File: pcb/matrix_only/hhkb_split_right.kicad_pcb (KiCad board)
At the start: 2 copper layers, 171.7 x 97.4 mm, 83 parts, among them SW1 CPG151101S11-2, SW10 CPG151101S11-2, SW11 CPG151101S11-2, SW12 CPG151101S11-2, SW13 CPG151101S11-2, SW14 CPG151101S11-2, SW15 CPG151101S11-2, SW16 CPG151101S11-2, SW17 CPG151101S11-2, SW18 CPG151101S11-2, SW19 CPG151101S11-2, SW2 CPG151101S11-2, SW20 CPG151101S11-2, SW21 CPG151101S11-2, SW22 CPG151101S11-2, SW23 CPG151101S11-2, SW24 CPG151101S11-2, SW25 CPG151101S11-2, SW26 CPG151101S11-2, SW27 CPG151101S11-2, SW28 CPG151101S11-2, SW29 CPG151101S11-2, SW3 CPG151101S11-2, SW30 CPG151101S11-2, SW31 CPG151101S11-2, SW32 CPG151101S11-2, SW33 CPG151101S11-2, SW34 CPG151101S11-2, SW4 CPG151101S11-2, SW5 CPG151101S11-2, SW6 CPG151101S11-2, SW7 CPG151101S11-2, SW8 CPG151101S11-2, SW9 CPG151101S11-2, U1 74LVC595, U2 74LVC595

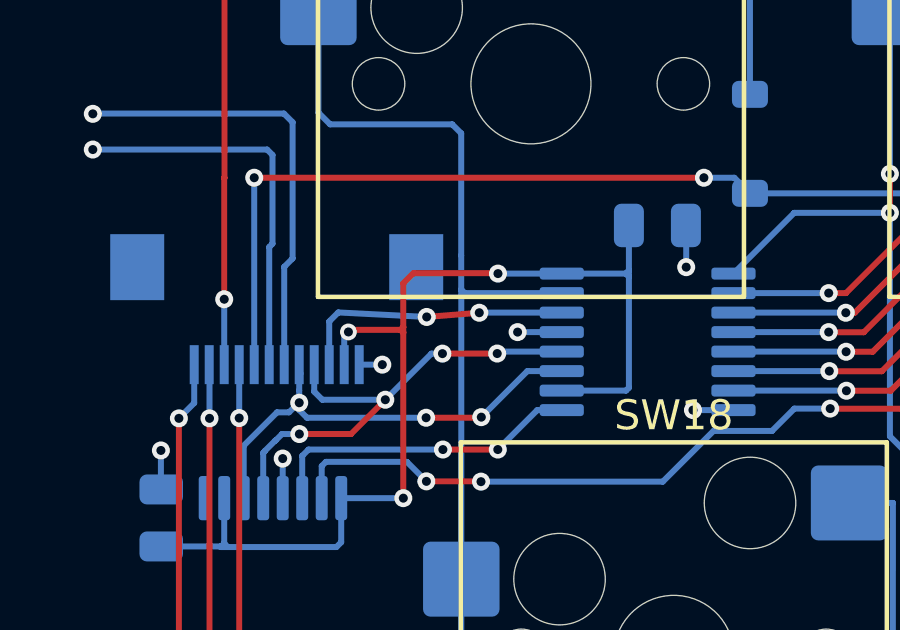
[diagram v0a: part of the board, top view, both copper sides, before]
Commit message: #49 左の SCK・CS・V3V3 にも露出ビア（利用者）。露出は左右の全ネットがビアに。3 基板 DRC 0・検査 460 緑
Co-Authored-By: Claude Fable 5 <noreply@anthropic.com>
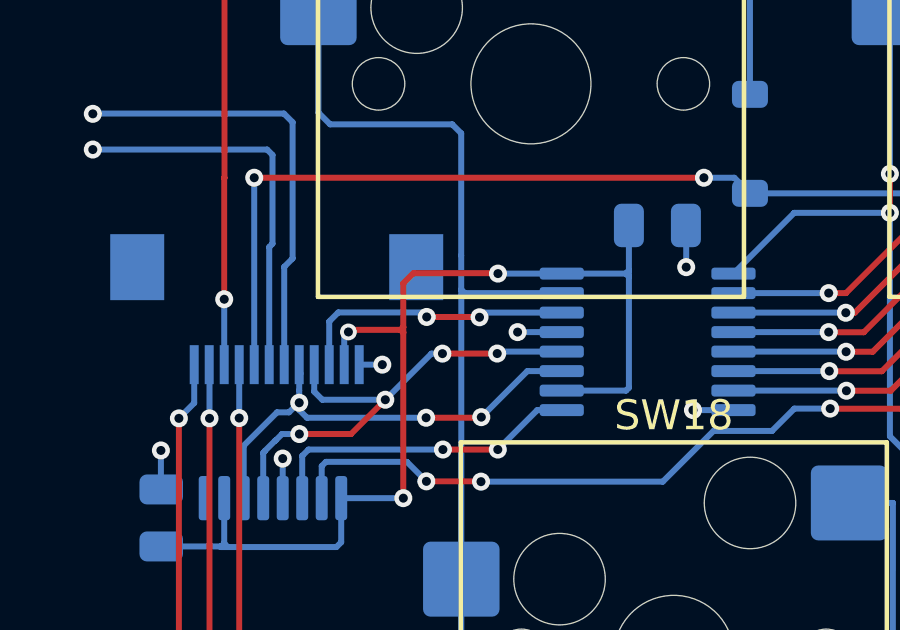
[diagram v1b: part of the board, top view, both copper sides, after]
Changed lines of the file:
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@@
 	(segment
 		(start 79.85 88.72)
-		(end 79.85 88.72)
+		(end 81.6 88.72)
+		(width 0.2)
+		(layer "F.Cu")
+		(net "SPI_MOSI")
+	)
+	(segment
+		(start 81.6 88.72)
+		(end 81.61 88.73)
 		(width 0.2)
 		(layer "F.Cu")
@@
 	(segment
 		(start 79.85 88.72)
-		(end 81.6025 88.58)
+		(end 79.85 88.72)
 		(width 0.2)
 		(layer "F.Cu")
@@
 	)
 	(via
-		(at 81.6025 88.58)
+		(at 81.61 88.73)
 		(size 0.6)
 		(drill 0.3)
@@
 	)
 	(segment
-		(start 76.6 90.309999)
-		(end 76.599999 90.31)
+		(start 79.7 88.57)
+		(end 79.85 88.72)
 		(width 0.2)
 		(layer "B.Cu")
@@
 	)
 	(segment
-		(start 81.815 88.575)
-		(end 84.3505 88.575)
-		(width 0.2)
-		(layer "B.Cu")
-		(net "SPI_MOSI")
-	)
-	(segment
-		(start 81.81 88.58)
-		(end 81.815 88.575)
+		(start 76.6 90.309999)
+		(end 76.599999 90.31)
 		(width 0.2)
 		(layer "B.Cu")
@@
 	)
 	(segment
-		(start 79.85 88.72)
-		(end 76.902182 88.57)
+		(start 81.765 88.575)
+		(end 84.3505 88.575)
 		(width 0.2)
 		(layer "B.Cu")
@@
 	)
 	(segment
-		(start 81.6025 88.58)
-		(end 81.81 88.58)
+		(start 81.61 88.73)
+		(end 81.765 88.575)
 		(width 0.2)
 		(layer "B.Cu")
+		(net "SPI_MOSI")
+	)
+	(segment
+		(start 76.902182 88.57)
+		(end 79.7 88.57)
+		(width 0.2)
+		(layer "B.Cu")

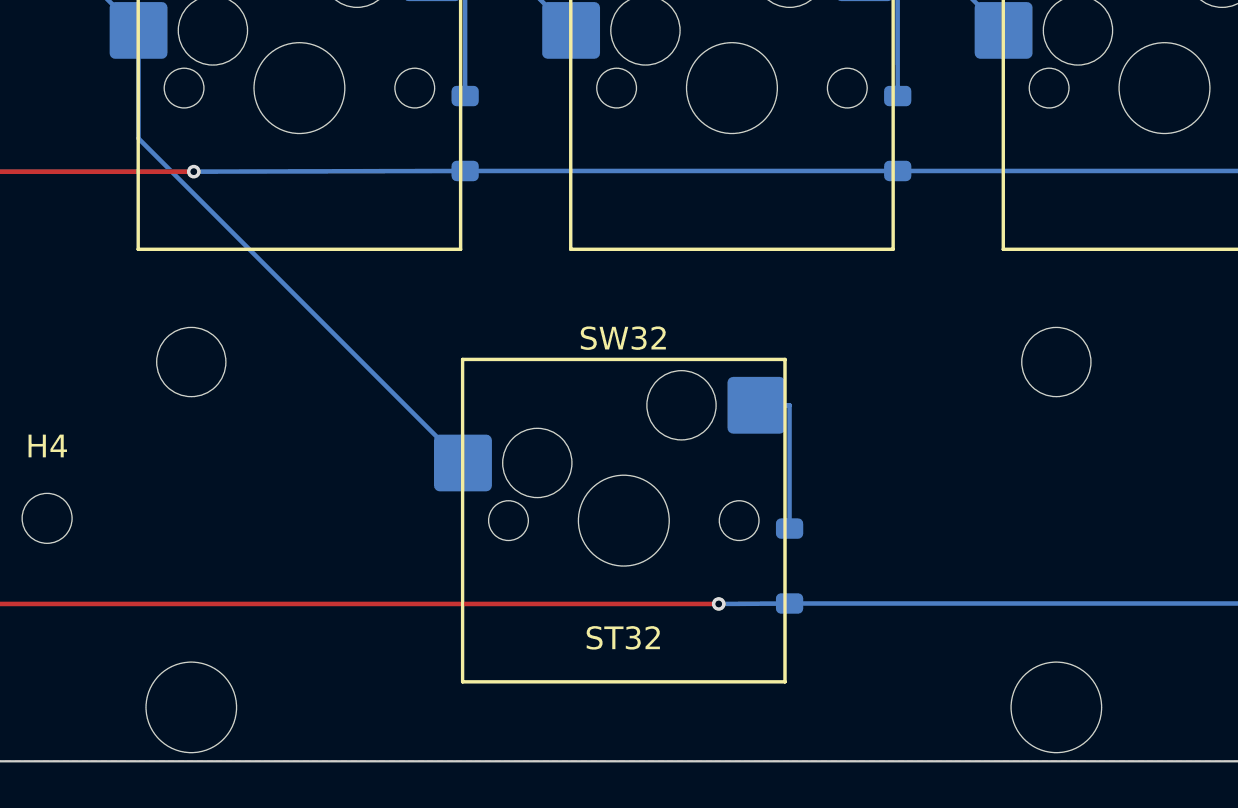
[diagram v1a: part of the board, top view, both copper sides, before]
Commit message: スペースキー 2.75u 化を基板まで反映（3 基板とも DRC 0 / 未配線 0）
設計側（29f4471）に続き、基板を作り直した。

**matrix_only のスペースキーを 2.75u へ**（KiCad の API で差し替え）:
- SW27/SW32 → SW_Hotswap_Kailh_MX_2.75u
- ST27/ST32 → Stabilizer_Cherry_MX_2.00u（穴が ±19.05 → ±11.938）
- SW/ST/D を x 左 −2.38125 / 右 +2.38125 だけ移動

**配線**: ダイオード側 2 本ずつは平行移動で端点がパッドに 0.0001mm 一致。
COL は経路の形が変わるので引き直した（左 COL3・右 COL0）。
⚠️ **利用者の指摘「col0 の配線が規則的じゃない」「col3 も」で 1 度やり直した。**
最初はクリアランスだけ見て 71.9°/2.6°/28.1°/82.9° の半端な角度で引いており、
**この板の他の配線は全部 0°/45°/90°/135°** だった。
縦→45°→水平の 3 区間に作り直し、角度を 45° の倍数に固定したまま
総当たりで障害物との距離が最大の経路を選んだ（左 +0.656mm / 右 +1.650mm）。

**シルクが 0.12mm のまま残っていたのも直した**（gen_pcb の仕上げを
通らないため。→ pcb-routing-handover.md に落とし穴として記録）。

検証: 3 基板とも 違反 0 / 未配線 0。スタビ 4 個すべて ±11.938。
STL のハウジング間隔を実測して 23.880mm（=2u）を確認。
fab_check（595 48 パッド / XIAO 14 パッド / 61 キー経路）全 OK。
基板の外形は不変（左 138.363×97.4 / 右 171.70×97.4 / 子 21.0×32.0）。
検査 464 緑。

記録: スタビの節を 2.75u 前提に書き直し、国内入手性の調査結果
（2u は潤沢・3u は買えない）と、FFC コネクタ C88360 の在庫が
40 日で 0 になるペースであることを追記。#46 の古い「次の一手」も直した。

Co-Authored-By: Claude Opus 5 (1M context) <noreply@anthropic.com>
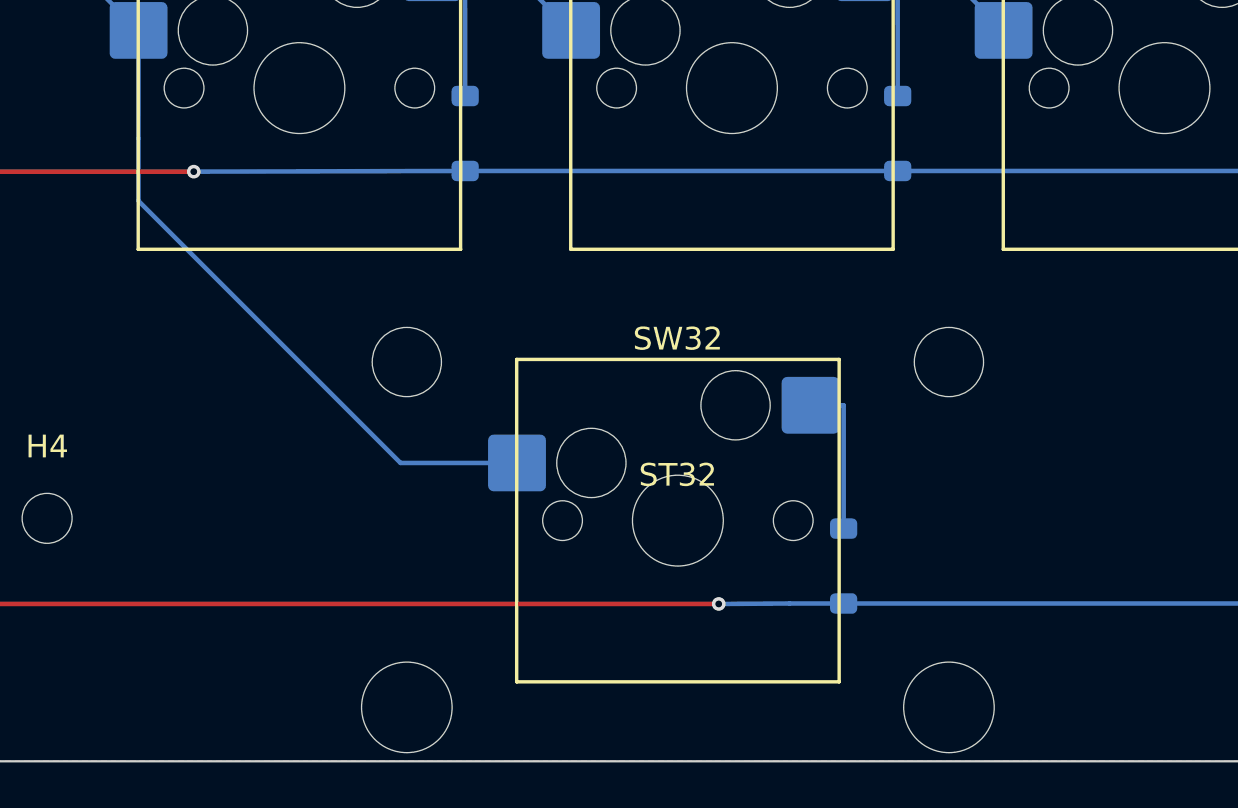
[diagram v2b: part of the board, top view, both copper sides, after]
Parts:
- ST32: value Stabilizer_Cherry_MX_3.00u -> Stabilizer_Cherry_MX_2.00u; footprint Stabilizer_Cherry_MX_3.00u -> Stabilizer_Cherry_MX_2.00u
- SW32: footprint SW_Hotswap_Kailh_MX_3.00u -> SW_Hotswap_Kailh_MX_2.75u
- moved D32 2.38 mm to (121.6, 140.1)
- moved ST32 2.38 mm to (114.3, 138.1)
- moved SW32 2.38 mm to (114.3, 138.1)
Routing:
- net COL0: track 97.9 -> 101.9 mm

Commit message: #53 決着: スペースのスタビ 2 個を 180°（ワイヤ奥）に回す。大穴が板前縁まで 0.381mm だったのが小穴 2.14mm に。interface.stab_flipped を gen_pcb・gen_plate・find_mounts が見る。matrix_only の ST27/ST32 を回して手順どおり再生成、3 基板 DRC 0・警告数不変。NPTH の縁 ≥1.0mm の検査を足し、回す前の板で 0.381 を検出することを確認。実形状のスタビ開口検査・test_assembly 69 件・高速 387 件緑
Co-Authored-By: Claude Fable 5 <noreply@anthropic.com>
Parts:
- turned ST32 to 180 degrees
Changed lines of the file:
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@@
 	(footprint "Stabilizer_Cherry_MX_2.00u"
 		(layer "F.Cu")
-		(at 114.28125 138.1)
+		(at 114.28125 138.1 180)
 		(descr "Cherry MX PCB Stabilizer 2.00u 2.25u 2.50u 2.75u")
 		(tags "Cherry MX Keyboard Stabilizer 2.00u 2.25u 2.50u 2.75u Cutout")
 		(property "Reference" "ST32"
-			(at 0 -2 0)
+			(at 0 -2 180)
 			(layer "F.SilkS")
 			(effects
@@
 		)
 		(property "Value" "Stabilizer_Cherry_MX_2.00u"
-			(at 0 2 0)
+			(at 0 2 180)
 			(layer "F.Fab")
 			(effects
@@
 		)
 		(property "Datasheet" ""
-			(at 0 0 0)
+			(at 0 0 180)
 			(layer "F.Fab")
 			(hide yes)
@@
 		)
 		(property "Description" ""
-			(at 0 0 0)
+			(at 0 0 180)
 			(layer "F.Fab")
 			(hide yes)
@@
 		(duplicate_pad_numbers_are_jumpers no)
 		(fp_line
+			(start 0 2)
+			(end 0 -2)
+			(stroke
+				(width 0.1)
+				(type solid)
+			)
+			(layer "Dwgs.User")
+		)
+		(fp_line
 			(start -2 0)
 			(end 2 0)
@@
 		)
 		(fp_line
-			(start 0 2)
-			(end 0 -2)
+			(start 15.313 6.77)
+			(end 15.313 -5.53)
 			(stroke
 				(width 0.1)
 				(type solid)
 			)
-			(layer "Dwgs.User")
+			(layer "Eco1.User")
 		)
 		(fp_line
-			(start -15.313 -5.53)
-			(end -15.313 6.77)
+			(start 15.313 -5.53)
+			(end 8.563 -5.53)
+			(stroke
+				(width 0.1)
+				(type solid)
+			)
+			(layer "Eco1.User")
+		)
+		(fp_line
+			(start 8.563 6.77)
+			(end 15.313 6.77)
+			(stroke
+				(width 0.1)
+				(type solid)
+			)
+			(layer "Eco1.User")
+		)
+		(fp_line
+			(start 8.563 -5.53)
+			(end 8.563 6.77)
+			(stroke
+				(width 0.1)
+				(type solid)
+			)
+			(layer "Eco1.User")
+		)
+		(fp_line
+			(start -8.563 6.77)
+			(end -8.563 -5.53)
+			(stroke
+				(width 0.1)
+				(type solid)
+			)
+			(layer "Eco1.User")
+		)
+		(fp_line
+			(start -8.563 -5.53)
+			(end -15.313 -5.53)
 			(stroke
 				(width 0.1)
@@
 		)
 		(fp_line
-			(start -8.563 -5.53)
-			(end -15.313 -5.53)
-			(stroke
-				(width 0.1)
-				(type solid)
-			)
-			(layer "Eco1.User")
-		)
-		(fp_line
-			(start -8.563 6.77)
-			(end -8.563 -5.53)
-			(stroke
-				(width 0.1)
-				(type solid)
-			)
-			(layer "Eco1.User")
-		)
-		(fp_line
-			(start 8.563 -5.53)
-			(end 8.563 6.77)
-			(stroke
-				(width 0.1)
-				(type solid)
-			)
-			(layer "Eco1.User")
-		)
-		(fp_line
-			(start 8.563 6.77)
-			(end 15.313 6.77)
-			(stroke
-				(width 0.1)
-				(type solid)
-			)
-			(layer "Eco1.User")
-		)
-		(fp_line
-			(start 15.313 -5.53)
-			(end 8.563 -5.53)
-			(stroke
-				(width 0.1)
-				(type solid)
-			)
-			(layer "Eco1.User")
-		)
-		(fp_line
-			(start 15.313 6.77)
-			(end 15.313 -5.53)
+			(start -15.313 -5.53)
+			(end -15.313 6.77)
 			(stroke
 				(width 0.1)
@@
 		)
 		(fp_text user "${REFERENCE}"
-			(at 0 0 0)
+			(at 0 0 180)
 			(layer "F.Fab")
 			(effects
@@
 		)
 		(pad "" np_thru_hole circle
-			(at -11.938 -6.985)
+			(at -11.938 -6.985 180)
 			(size 3.048 3.048)
 			(drill 3.048)
@@
 		)
 		(pad "" np_thru_hole circle
-			(at -11.938 8.225)
+			(at -11.938 8.225 180)
 			(size 3.9878 3.9878)
 			(drill 3.9878)
@@
 		)
 		(pad "" np_thru_hole circle
-			(at 11.938 -6.985)
+			(at 11.938 -6.985 180)
 			(size 3.048 3.048)
 			(drill 3.048)
@@
 		)
 		(pad "" np_thru_hole circle
-			(at 11.938 8.225)
+			(at 11.938 8.225 180)
 			(size 3.9878 3.9878)
 			(drill 3.9878)

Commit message: open-gaps #56: スペースを両島の内側端へ寄せ直し（左 4.5〜7.25u・右 9.75〜12.5u、Meta との空き左右対称 0.5u）
- layout: 最下段のみ。Alt 1u / Meta 1.5u は原機の位置のまま（利用者確認）
- 基板の柱 左 H2 (64,−30)・右 H4 (−81,−38)。柱がキーの真下に立つ取り違えを
  test_pcb_posts_do_not_touch_any_key で見る（H4 を戻すと落ちる）
- matrix_only: SW27/ST27/D27・SW32/ST32/D32 を API で移動し配線を引き直し。
  キー名シルクは部品に付いてこないので手で移動（handover の「落ちる穴」に追記）
- export_matrix_routing → gen_pcb → finalize_pcb → pcb_parts → drc。
  3 基板 DRC 0 / 未配線 0、警告は元の 37 / 41 / 1。スタビ同心 0.000・180°・縁 2.14mm
- #21: DSA 1u/1.5u/1.75u/2.25u/2.75u が SP 直販で単品・在庫ありと確認。
  2.75u の外側マウント 0.469"＝11.9mm は Cherry 2u スタビと一致
- pytest 479 passed

Co-Authored-By: Claude Fable 5 <noreply@anthropic.com>
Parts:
- moved H4 17.5 mm to (69.0, 138.0)
- moved D32 9.53 mm to (112.1, 140.1)
- moved ST32 9.53 mm to (104.8, 138.1)
- moved SW32 9.53 mm to (104.8, 138.1)
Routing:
- net COL0: track 101.9 -> 95.0 mm
- net ROW_E: track 165.8 -> 169.8 mm
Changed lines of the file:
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@@
 	(footprint "Stabilizer_Cherry_MX_2.00u"
 		(layer "F.Cu")
-		(at 114.28125 138.1 180)
+		(at 104.75625 138.1 180)
 		(descr "Cherry MX PCB Stabilizer 2.00u 2.25u 2.50u 2.75u")
 		(tags "Cherry MX Keyboard Stabilizer 2.00u 2.25u 2.50u 2.75u Cutout")
@@
 	(footprint "SW_Hotswap_Kailh_MX_2.75u"
 		(layer "F.Cu")
-		(at 114.28125 138.1)
+		(at 104.75625 138.1)
 		(descr "Kailh keyswitch Hotswap Socket Keycap 2.75u")
 		(tags "Kailh Keyboard Keyswitch Switch Hotswap Socket Relief Cutout Keycap 2.75u")
@@
 	(footprint "MountingHole_2.2mm_M2"
 		(layer "F.Cu")
-		(at 86.5 138)
+		(at 69 138)
 		(descr "Mounting Hole 2.2mm, M2, no annular, generated by kicad-footprint-generator mountinghole.py")
 		(tags "mountinghole M2")
@@
 	(footprint "D_SOD-123"
 		(layer "B.Cu")
-		(at 121.58125 140.1 90)
+		(at 112.056249 140.1 90)
 		(descr "SOD-123")
 		(tags "SOD-123")
@@
 		)
 	)
-	(gr_text "J"
-		(at 107.137499 91.8 0)
+	(gr_text "R-Space"
+		(at 104.75625 129.9 0)
 		(layer "B.SilkS")
 		(effects
@@
 		)
 	)
-	(gr_text "8"
-		(at 111.9 53.699999 0)
+	(gr_text "J"
+		(at 107.137499 91.8 0)
 		(layer "B.SilkS")
 		(effects
@@
 		)
 	)
-	(gr_text "R-Space"
-		(at 111.9 129.9 0)
+	(gr_text "8"
+		(at 111.9 53.699999 0)
 		(layer "B.SilkS")
 		(effects
@@
 	)
 	(segment
+		(start 97.67125 131.166249)
+		(end 97.67125 135.56)
+		(width 0.2)
+		(layer "B.Cu")
+		(net "COL0")
+	)
+	(segment
 		(start 81 82.6)
 		(end 80.7 82.3)
@@
 	(segment
 		(start 90.525 124.02)
-		(end 102.065 135.56)
+		(end 97.67125 131.166249)
 		(width 0.2)
 		(layer "B.Cu")
@@
 	)
 	(segment
-		(start 102.065 135.56)
-		(end 107.1963 135.56)
-		(width 0.2)
-		(layer "B.Cu")
-		(net "COL0")
-	)
-	(segment
 		(start 76.24 72.385)
 		(end 66.715 62.86)
@@
 	)
 	(segment
-		(start 121.58125 133.02)
-		(end 121.58125 138.45)
+		(start 110.59825 133.02)
+		(end 112.056249 133.02)
 		(width 0.2)
 		(layer "B.Cu")
@@
 	)
 	(segment
-		(start 120.12325 133.02)
-		(end 121.58125 133.02)
+		(start 112.056249 133.02)
+		(end 112.056249 138.45)
 		(width 0.2)
 		(layer "B.Cu")
@@
 		(width 0.2)
 		(layer "B.Cu")
+		(net "ROW_E")
+	)
+	(segment
+		(start 112.056249 141.75)
+		(end 116.08 141.77)
+		(width 0.2)
+		(layer "B.Cu")
